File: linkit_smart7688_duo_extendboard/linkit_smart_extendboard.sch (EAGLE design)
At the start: 25 parts, among them U1 BME280

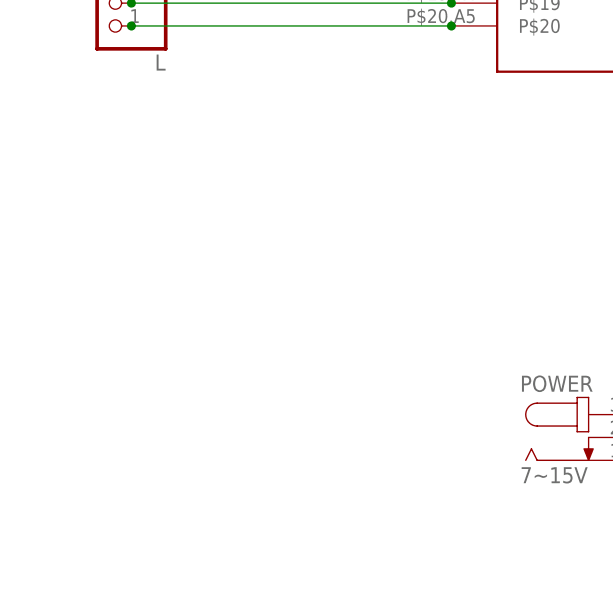
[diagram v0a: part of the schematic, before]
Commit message: update PCB layout,prepare for future box design
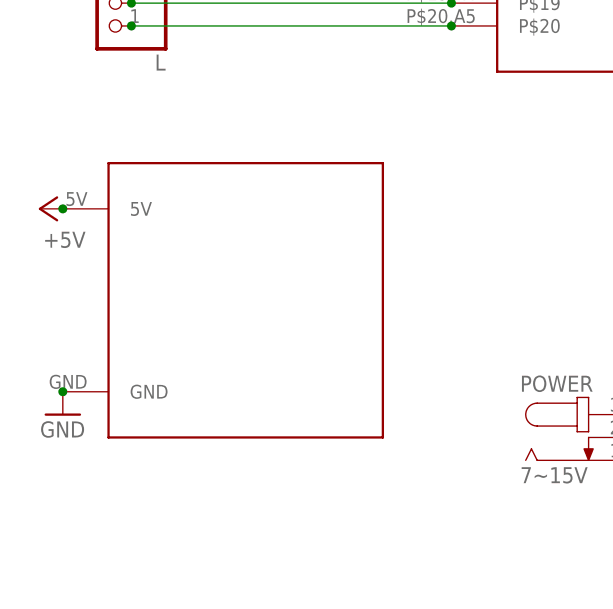
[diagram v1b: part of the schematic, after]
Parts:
- added U$4: PIN2MM, pin_2mm:PIN2MM
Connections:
- net +5V: now also U$4.5V
- net GND: now also U$4.GND
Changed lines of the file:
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@@
 </class>
 </classes>
+<modules>
+<module name="PIN" prefix="" dx="30.48" dy="20.32">
+<ports>
+</ports>
+<variantdefs>
+</variantdefs>
+<parts>
+</parts>
+<sheets>
+<sheet>
+<plain>
+</plain>
+<instances>
+</instances>
+<busses>
+</busses>
+<nets>
+</nets>
+</sheet>
+</sheets>
+</module>
+</modules>
 <parts>
 <part name="U$1" library="linkit7688" deviceset="LINKIT7688" device=""/>
@@
 <part name="+3V6" library="supply1" deviceset="+3V3" device=""/>
 <part name="+3V7" library="supply1" deviceset="+3V3" device=""/>
+<part name="U$4" library="pin_2mm" deviceset="PIN2MM" device=""/>
+<part name="P+6" library="supply1" deviceset="+5V" device=""/>
+<part name="GND23" library="supply1" deviceset="GND" device=""/>
 </parts>
 <sheets>
@@
 <instance part="+3V6" gate="G$1" x="76.2" y="27.94" rot="R90"/>
 <instance part="+3V7" gate="G$1" x="76.2" y="12.7" rot="R90"/>
+<instance part="U$4" gate="G$1" x="-66.04" y="-15.24"/>
+<instance part="P+6" gate="1" x="-73.66" y="10.16" rot="R90"/>
+<instance part="GND23" gate="1" x="-71.12" y="-12.7"/>
 </instances>
 <busses>
@@
 <junction x="83.82" y="-7.62"/>
 </segment>
+<segment>
+<pinref part="U$4" gate="G$1" pin="5V"/>
+<pinref part="P+6" gate="1" pin="+5V"/>
+<junction x="-71.12" y="10.16"/>
+</segment>
 </net>
 <net name="+3V3" class="0">
@@
 <junction x="167.64" y="93.98"/>
 </segment>
+<segment>
+<pinref part="U$4" gate="G$1" pin="GND"/>
+<pinref part="GND23" gate="1" pin="GND"/>
+<junction x="-71.12" y="-10.16"/>
+</segment>
 </net>
